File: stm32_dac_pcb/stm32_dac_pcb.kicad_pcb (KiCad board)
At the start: 2 copper layers, 64.3 x 21.8 mm, 47 parts, among them J201 Conn_01x03, J202 Conn_01x05, J204 USB_C_Receptacle_USB2.0, J301 AudioJack4, SW201 SW_Push, SW202 SW_Push, SW203 SW_Push, U101 AP1117-33, U102 AP1117-33, U201 STM32F411CEUx, U301 PCM5102A

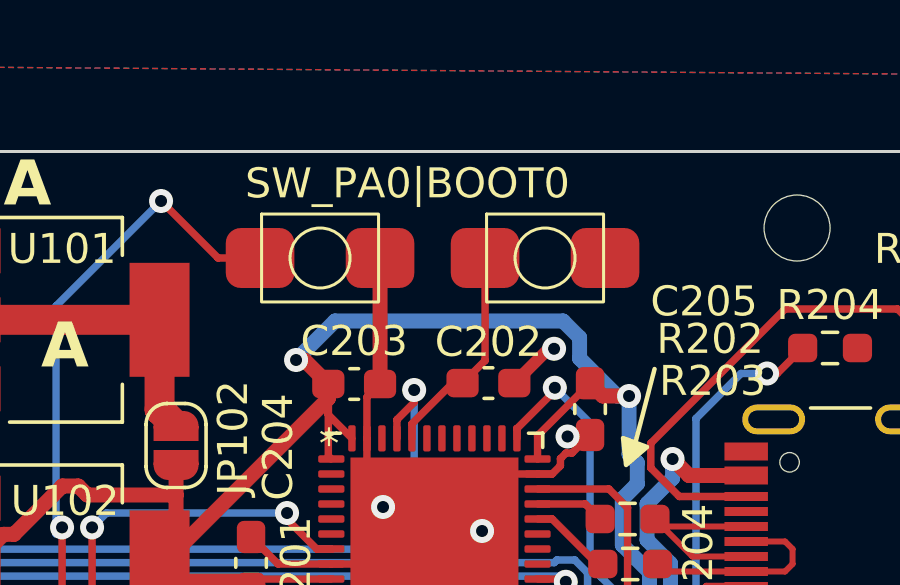
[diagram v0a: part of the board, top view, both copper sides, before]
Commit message: Add LED, layout
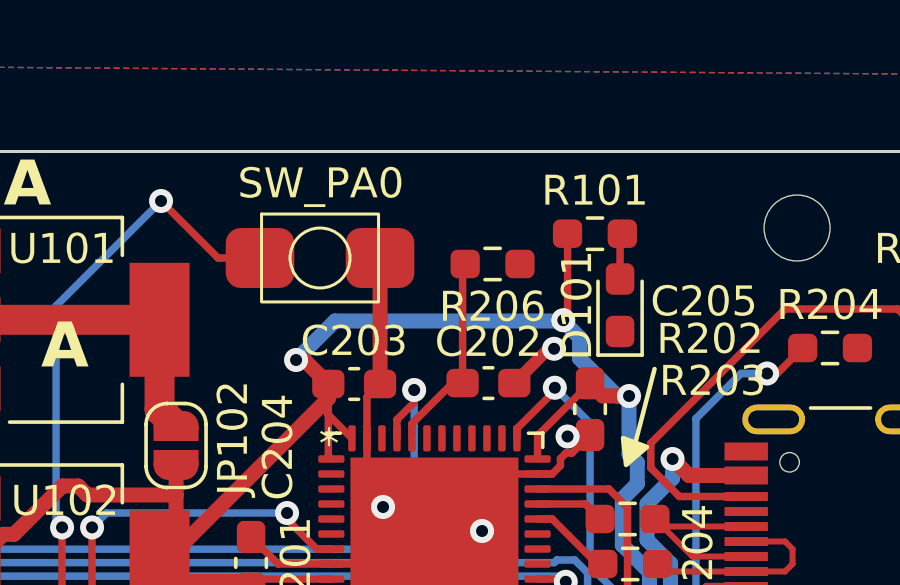
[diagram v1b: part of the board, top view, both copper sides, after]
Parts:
- removed SW203: SW_Push, 0_project_fp_lib:PushButtonSMD_2.93x3.9
- added D101: LED, LED_SMD:LED_0603_1608Metric_Pad1.05x0.95mm_HandSolder, F.Cu at (148.0, 90.4)
- added R101: 5k1, Resistor_SMD:R_0603_1608Metric_Pad0.98x0.95mm_HandSolder, F.Cu at (147.2, 88.0)
- added R206: 10k, Resistor_SMD:R_0603_1608Metric_Pad0.98x0.95mm_HandSolder, F.Cu at (143.8, 89.0)
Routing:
- net +3.3V: track 106.0 -> 109.0 mm, vias 4 -> 5
- net Net-(D101-A): track 0.00 -> 1.54 mm
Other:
- board text added: "SW_PA0"
- board text removed: "SW_PA0|BOOT0"

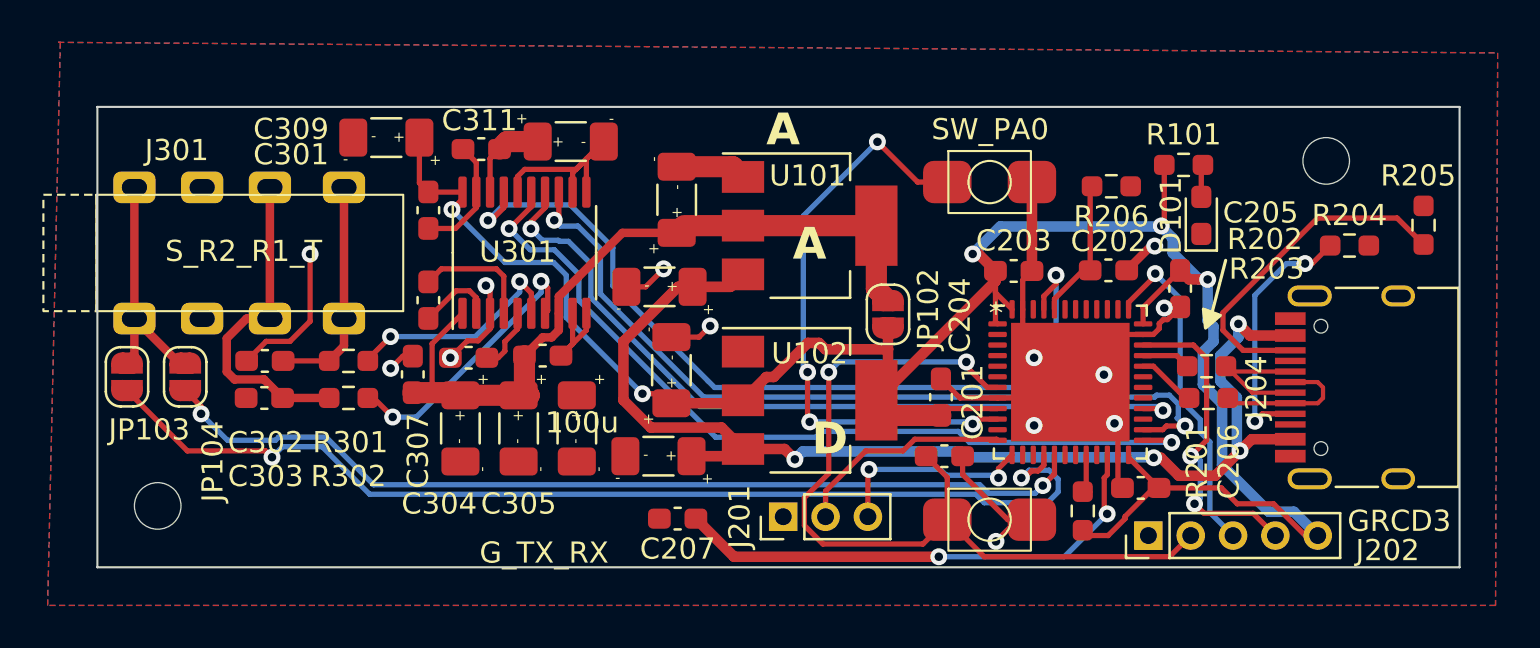
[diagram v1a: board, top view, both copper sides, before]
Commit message: Finish layout with crystal
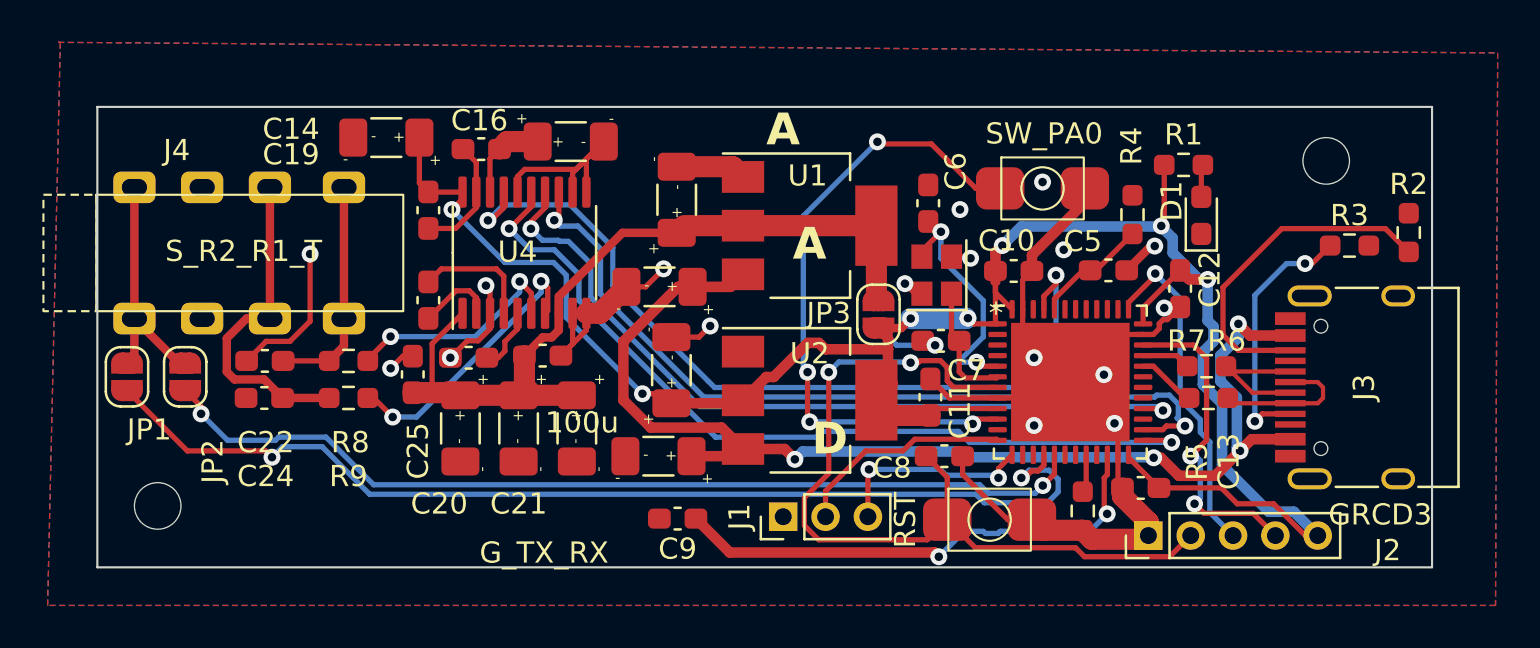
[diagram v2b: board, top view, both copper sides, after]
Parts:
- added C6: 12p, Capacitor_SMD:C_0603_1608Metric_Pad1.08x0.95mm_HandSolder, F.Cu at (135.1, 89.8)
- added C7: 12p, Capacitor_SMD:C_0603_1608Metric_Pad1.08x0.95mm_HandSolder, F.Cu at (135.7, 96.3)
- added Y1: 25MHz, 9pF, Crystal:Crystal_SMD_2520-4Pin_2.5x2.0mm, F.Cu at (135.5, 93.2)
- moved SW2 2.52 mm to (140.5, 89.1)
- moved R4 1.67 mm to (144.8, 90.3), turned to -90 degrees
- moved R2 0.78 mm to (157.8, 91.2)
- moved C11 0.50 mm to (135.2, 99.0)
- moved JP3 0.45 mm to (132.8, 95.0)
- renumbered C101 to C1, C203 to C10, C204 to C11, C205 to C12, C206 to C13, C309 to C14, C310 to C15, C311 to C16, C312 to C17, C313 to C18, C301 to C19, C102 to C2, C304 to C20, C305 to C21, C302 to C22, C306 to C23, C303 to C24, C307 to C25, C308 to C26, C103 to C3, C104 to C4, C202 to C5, C201 to C8, C207 to C9, D101 to D1, H101 to H1, H102 to H2, J201 to J1, J202 to J2, J204 to J3, J301 to J4, JP103 to JP1, JP104 to JP2, JP102 to JP3, R101 to R1, R205 to R2, R204 to R3, R206 to R4, R201 to R5, R203 to R6, R202 to R7, R301 to R8, R302 to R9, SW202 to SW1, SW201 to SW2, U101 to U1, U102 to U2, U201 to U3, U301 to U4
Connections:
- R5 pad 1: +3.3V -> GND
- U3 pad 5: unconnected-(U201-PH0-Pad5) -> Net-(U3-PH0)
- U3 pad 6: unconnected-(U201-PH1-Pad6) -> Net-(U3-PH1)
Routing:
- net GND: track 82.7 -> 97.6 mm, vias 13 -> 18
- net Net-(U3-PH0): track 0.00 -> 11.8 mm, vias 0 -> 2
- net +3.3V: track 109.0 -> 100.9 mm, vias 5 -> 7
- net Net-(U3-PH1): track 0.00 -> 5.79 mm
- net Net-(U3-PA0): track 28.3 -> 31.0 mm
- net +3.3VA: track 37.3 -> 39.9 mm
- net Net-(U3-BOOT0): track 6.74 -> 5.45 mm
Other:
- board size 64.3 x 21.8 mm -> 63.1 x 21.8 mm
- board text added: "RST"
- board text added: "Rev 2 2024-10-22 STM32 DAC DeflateAwning"
- board text removed: "Rev 1 2024-01-01 STM32 DAC DeflateAwning"
